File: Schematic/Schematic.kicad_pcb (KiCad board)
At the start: 2 copper layers, 139.7 x 114.3 mm, 16 parts, among them J1 S2B-PH-K-S_LF__SN_, P1 282837-2, P2 282837-2, U1 NRF52840-DONGLE, U3 LM1117DT-3.3, U4 YAAJ_DCDC_StepDown_LM2596

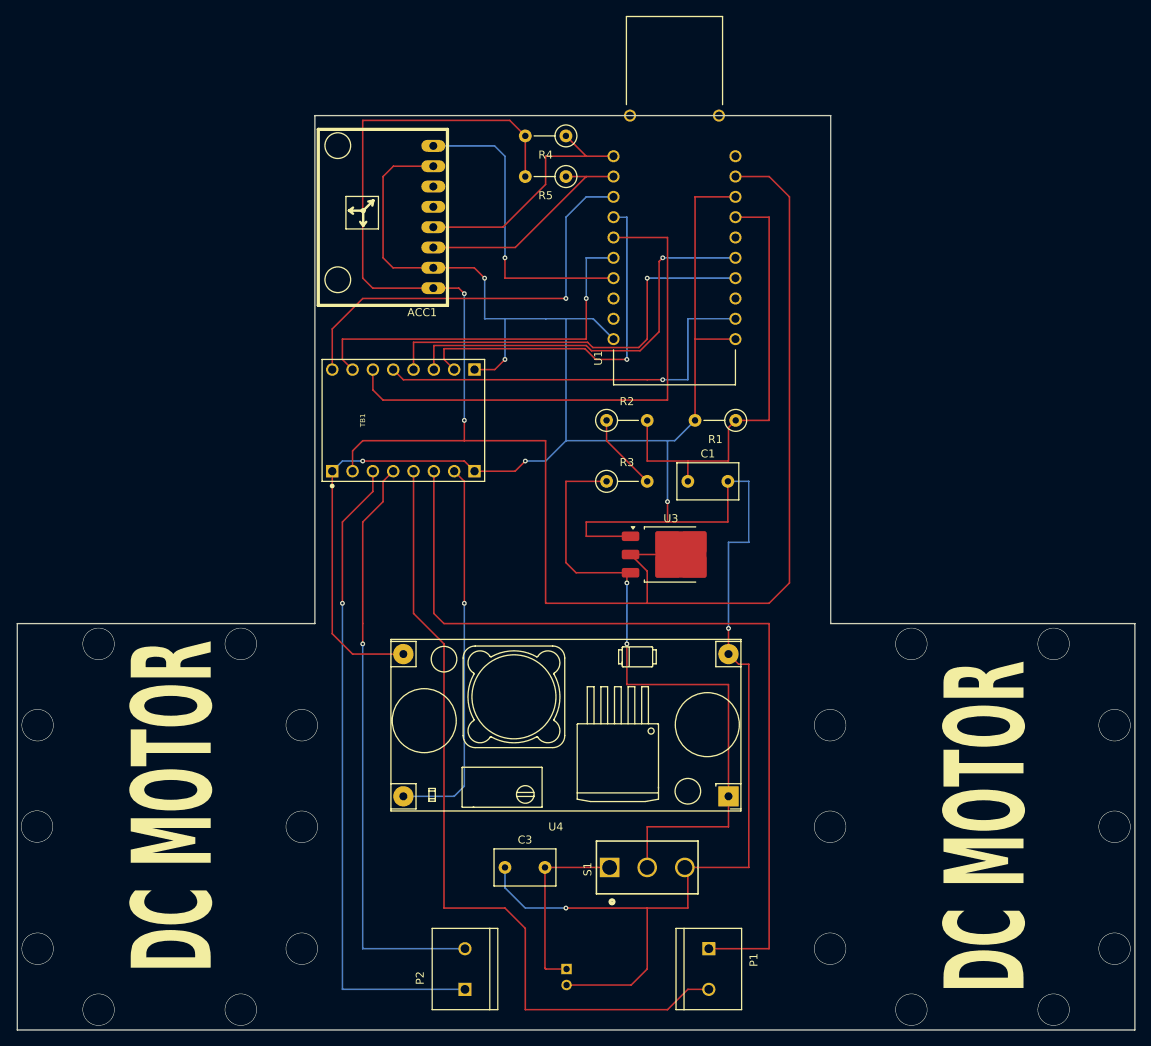
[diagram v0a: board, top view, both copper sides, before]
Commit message: schematic: added robot case model
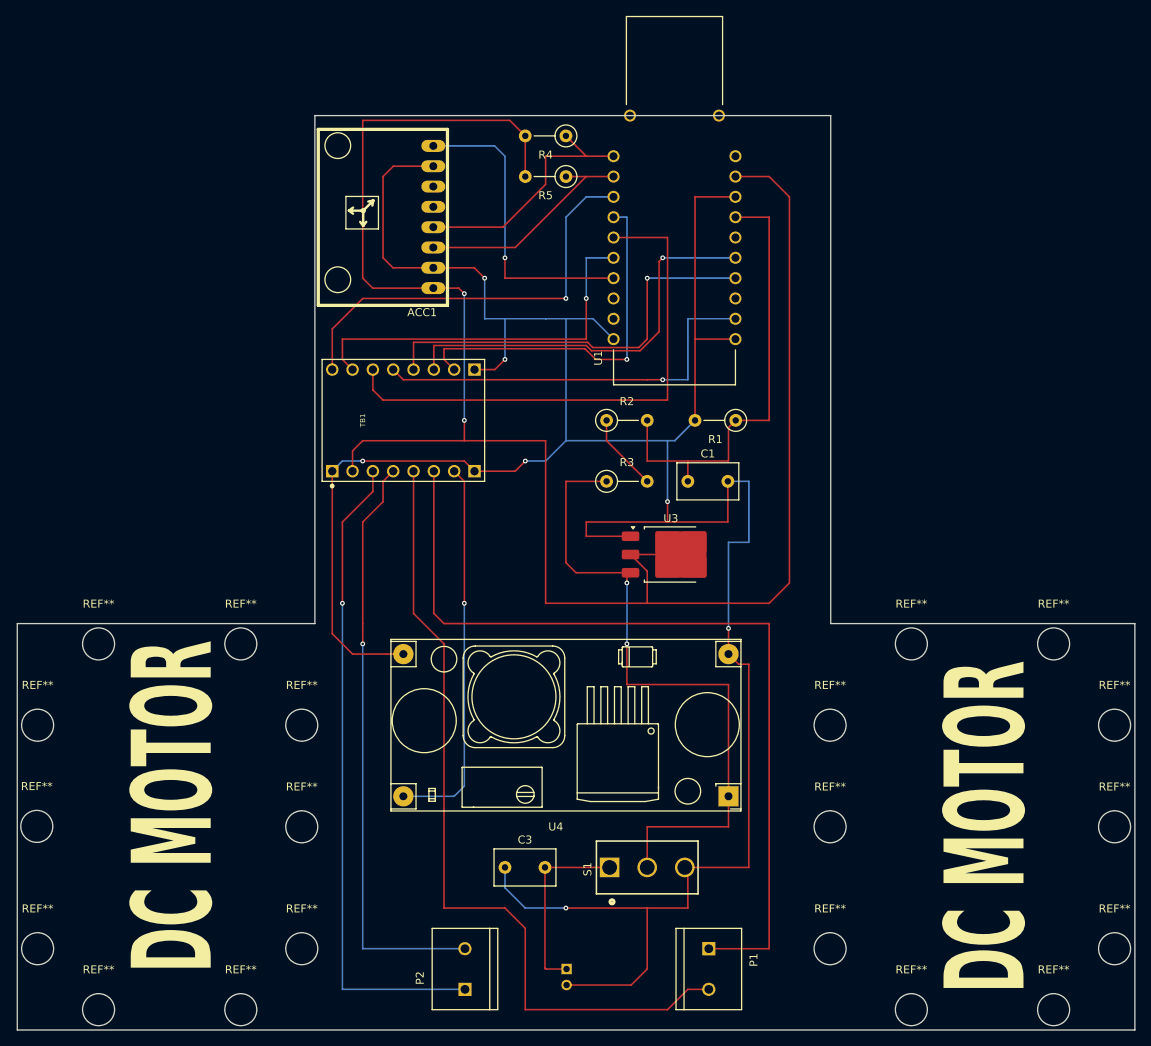
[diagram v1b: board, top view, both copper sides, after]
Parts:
- added REF**: MountingHole_4mm, MountingHole:MountingHole_4mm, F.Cu at (96.5, 149.9)
- added REF**: MountingHole_4mm, MountingHole:MountingHole_4mm, F.Cu at (71.1, 142.2)
- added REF**: MountingHole_4mm, MountingHole:MountingHole_4mm, F.Cu at (104.1, 114.3)
- added REF**: MountingHole_4mm, MountingHole:MountingHole_4mm, F.Cu at (180.3, 104.1)
- added REF**: MountingHole_4mm, MountingHole:MountingHole_4mm, F.Cu at (71.0, 126.9)
- added REF**: MountingHole_4mm, MountingHole:MountingHole_4mm, F.Cu at (78.7, 149.9)
- added REF**: MountingHole_4mm, MountingHole:MountingHole_4mm, F.Cu at (205.7, 127.0)
- added REF**: MountingHole_4mm, MountingHole:MountingHole_4mm, F.Cu at (104.1, 142.2)
- added REF**: MountingHole_4mm, MountingHole:MountingHole_4mm, F.Cu at (198.1, 149.9)
- added REF**: MountingHole_4mm, MountingHole:MountingHole_4mm, F.Cu at (170.2, 127.0)
- added REF**: MountingHole_4mm, MountingHole:MountingHole_4mm, F.Cu at (104.1, 127.0)
- added REF**: MountingHole_4mm, MountingHole:MountingHole_4mm, F.Cu at (71.1, 114.3)
- added REF**: MountingHole_4mm, MountingHole:MountingHole_4mm, F.Cu at (170.2, 142.2)
- added REF**: MountingHole_4mm, MountingHole:MountingHole_4mm, F.Cu at (205.7, 114.3)
- added REF**: MountingHole_4mm, MountingHole:MountingHole_4mm, F.Cu at (180.3, 149.9)
- added REF**: MountingHole_4mm, MountingHole:MountingHole_4mm, F.Cu at (78.7, 104.1)
- added REF**: MountingHole_4mm, MountingHole:MountingHole_4mm, F.Cu at (205.7, 142.2)
- added REF**: MountingHole_4mm, MountingHole:MountingHole_4mm, F.Cu at (96.5, 104.1)
- added REF**: MountingHole_4mm, MountingHole:MountingHole_4mm, F.Cu at (170.2, 114.3)
- added REF**: MountingHole_4mm, MountingHole:MountingHole_4mm, F.Cu at (198.1, 104.1)
